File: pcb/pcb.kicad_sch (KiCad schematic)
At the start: 7 parts

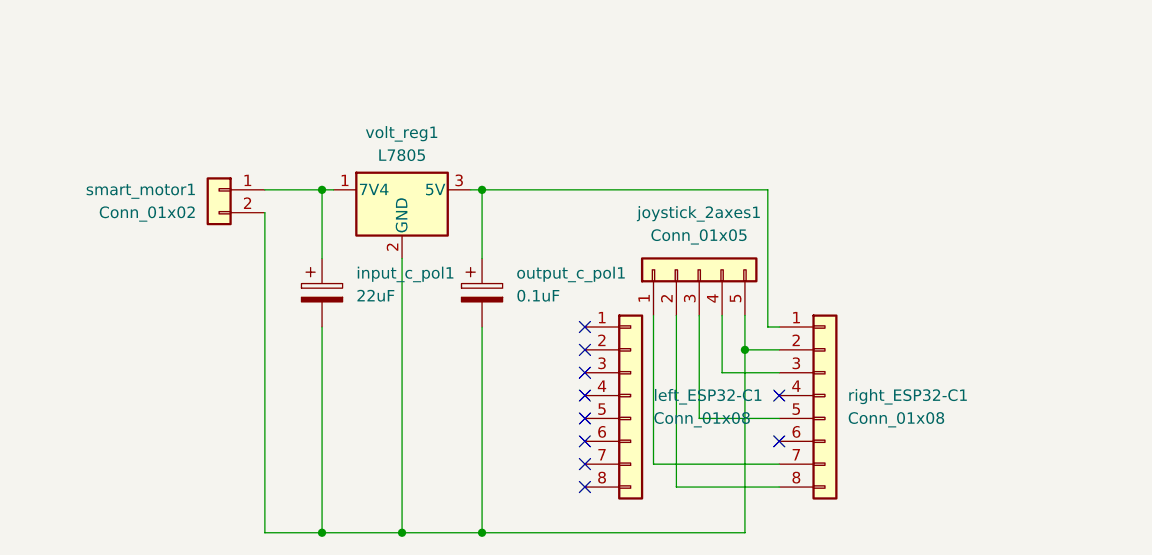
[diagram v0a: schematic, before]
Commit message: added ground plane on front and back of pcb
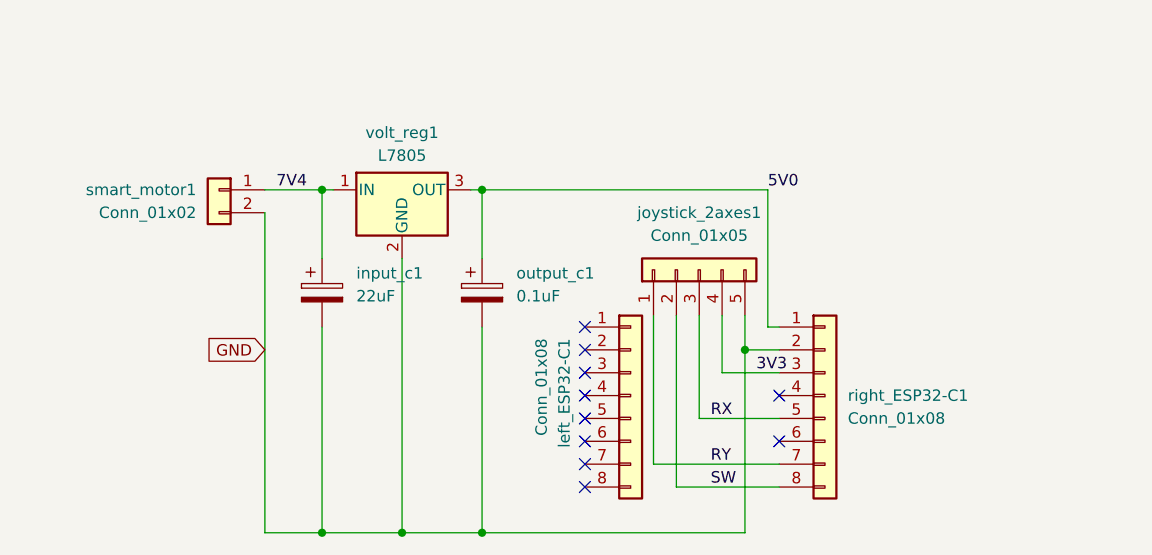
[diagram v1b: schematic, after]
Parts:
- output_c1: renamed from output_c_pol1; footprint Capacitor_THT:CP_Radial_D6.3mm_P2.50mm -> Capacitor_THT:CP_Radial_D4.0mm_P2.00mm
- renumbered input_c_pol1 to input_c1
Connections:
- net 7V4: now reaches input_c1.1, smart_motor1.1 (7V4), volt_reg1.1 (IN)
- net GND: now reaches input_c1.2, joystick_2axes1.5 (GND), output_c1.2, right_ESP32-C1.2 (GND), smart_motor1.2 (GND), volt_reg1.2 (GND)
- net 5V0: now reaches output_c1.1, right_ESP32-C1.1 (5V), volt_reg1.3 (OUT)
- net 3V3: now reaches joystick_2axes1.4 (5V), right_ESP32-C1.3 (3V3)
- net RX: now reaches joystick_2axes1.3 (Rx), right_ESP32-C1.5 (3)
- net RY: now reaches joystick_2axes1.1 (SW), right_ESP32-C1.7 (1)
- net SW: now reaches joystick_2axes1.2 (Ry), right_ESP32-C1.8 (0)
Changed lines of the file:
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@@
+	(wire
+		(pts
+			(xy 134.62 97.79) (xy 148.59 97.79)
+		)
+		(stroke
+			(width 0)
+			(type default)
+		)
+	)
 	(wire
 		(pts
@@
 	(wire
 		(pts
-			(xy 148.59 97.79) (xy 134.62 97.79)
-		)
-		(stroke
-			(width 0)
-			(type default)
-		)
-	)
-	(wire
-		(pts
 			(xy 144.78 81.28) (xy 144.78 85.09)
 		)
@@
 			(width 0)
 			(type default)
+		)
+	)
+	(label "7V4"
+		(at 92.71 67.31 0)
+		(effects
+			(font
+				(size 1.27 1.27)
+			)
+			(justify left bottom)
+		)
+	)
+	(label "RX"
+		(at 140.97 92.71 0)
+		(effects
+			(font
+				(size 1.27 1.27)
+			)
+			(justify left bottom)
+		)
+	)
+	(label "SW"
+		(at 140.97 100.33 0)
+		(effects
+			(font
+				(size 1.27 1.27)
+			)
+			(justify left bottom)
+		)
+	)
+	(label "3V3"
+		(at 146.05 87.63 0)
+		(effects
+			(font
+				(size 1.27 1.27)
+			)
+			(justify left bottom)
+		)
+	)
+	(label "RY"
+		(at 140.97 97.79 0)
+		(effects
+			(font
+				(size 1.27 1.27)
+			)
+			(justify left bottom)
+		)
+	)
+	(label "5V0"
+		(at 147.32 67.31 0)
+		(effects
+			(font
+				(size 1.27 1.27)
+			)
+			(justify left bottom)
+		)
+	)
+	(global_label "GND"
+		(shape input)
+		(at 91.44 85.09 180)
+		(fields_autoplaced yes)
+		(effects
+			(font
+				(size 1.27 1.27)
+			)
+			(justify right)
+		)
+		(property "Intersheetrefs" "${INTERSHEET_REFS}"
+			(at 84.5843 85.09 0)
+			(effects
+				(font
+					(size 1.27 1.27)
+				)
+				(justify right)
+				(hide yes)
+			)
 		)
 	)
@@
 		(dnp no)
 		(fields_autoplaced yes)
-		(property "Reference" "input_c_pol1"
+		(property "Reference" "input_c1"
 			(at 101.6 76.5809 0)
 			(effects
@@
 			(project ""
 				(path "/cf52163e-048c-48d9-89ec-e5d76936dc02"
-					(reference "input_c_pol1")
+					(reference "input_c1")
 					(unit 1)
 				)
@@
 		(dnp no)
 		(property "Reference" "left_ESP32-C1"
-			(at 134.62 90.1699 0)
-			(effects
-				(font
-					(size 1.27 1.27)
-				)
-				(justify left)
+			(at 124.714 83.82 90)
+			(effects
+				(font
+					(size 1.27 1.27)
+				)
+				(justify right)
 			)
 		)
 		(property "Value" "Conn_01x08"
-			(at 134.62 92.7099 0)
-			(effects
-				(font
-					(size 1.27 1.27)
-				)
-				(justify left)
+			(at 122.174 83.82 90)
+			(effects
+				(font
+					(size 1.27 1.27)
+				)
+				(justify right)
 			)
 		)
@@
 		(dnp no)
 		(fields_autoplaced yes)
-		(property "Reference" "output_c_pol1"
+		(property "Reference" "output_c1"
 			(at 119.38 76.5809 0)
 			(effects
@@
 			)
 		)
-		(property "Footprint" "Capacitor_THT:CP_Radial_D6.3mm_P2.50mm"
+		(property "Footprint" "Capacitor_THT:CP_Radial_D4.0mm_P2.00mm"
 			(at 116.5352 82.55 0)
 			(effects
@@
 			(project "pcb"
 				(path "/cf52163e-048c-48d9-89ec-e5d76936dc02"
-					(reference "output_c_pol1")
+					(reference "output_c1")
 					(unit 1)
 				)

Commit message: new pcb with custom footprint
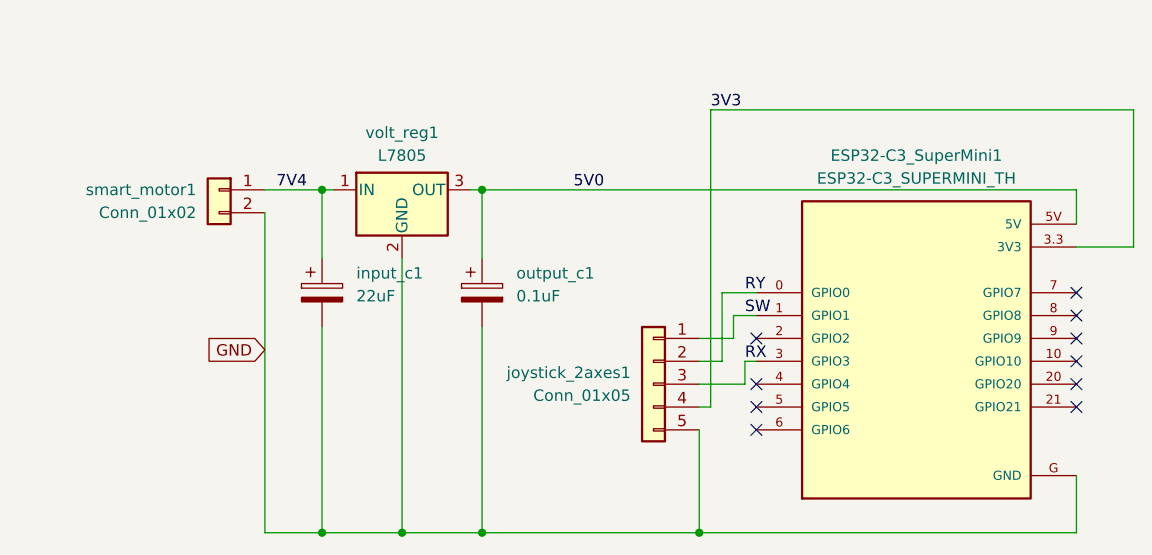
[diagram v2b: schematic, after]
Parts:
- removed left_ESP32-C1, right_ESP32-C1: Conn_01x08, Connector_PinSocket_2.54mm:PinSocket_1x08_P2.54mm_Vertical, symbol Connector_Generic:Conn_01x08
- added ESP32-C3_SuperMini1: ESP32-C3_SUPERMINI_TH, ESP32-C3_SUPERMINI_TH:MODULE_ESP32-C3_SUPERMINI_TH, symbol ESP32-C3_SUPERMINI_TH:ESP32-C3_SUPERMINI_TH
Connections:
- net 3V3: now also ESP32-C3_SuperMini1.3.3 (3V3)
- net 5V0: now also ESP32-C3_SuperMini1.5V
- net GND: now also ESP32-C3_SuperMini1.G (GND)
- net RX: now also ESP32-C3_SuperMini1.3 (GPIO3)
- net RY: now also joystick_2axes1.2 (Ry), ESP32-C3_SuperMini1.0 (GPIO0); no longer joystick_2axes1.1 (SW)
- net SW: now also joystick_2axes1.1 (SW), ESP32-C3_SuperMini1.1 (GPIO1); no longer joystick_2axes1.2 (Ry)
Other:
- moved on the sheet: joystick_2axes1

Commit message: added rounded edges, mounting holes and legend on pcb
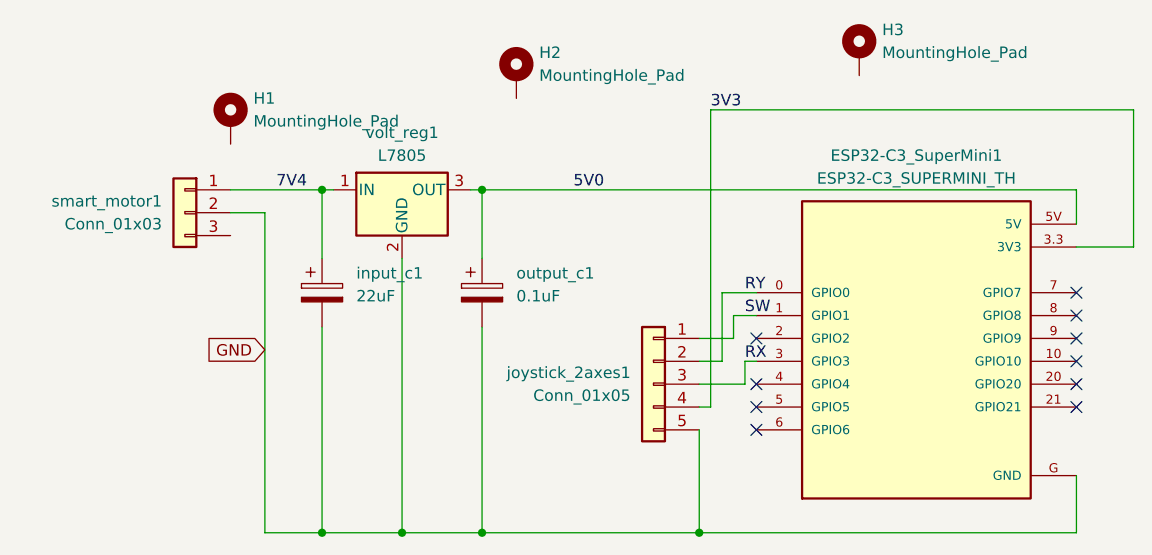
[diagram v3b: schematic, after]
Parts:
- removed smart_motor1: Conn_01x02, Connector_PinHeader_2.54mm:PinHeader_1x02_P2.54mm_Vertical, symbol Connector_Generic:Conn_01x02
- added H1, H2, H3: MountingHole_Pad, MountingHole:MountingHole_2.5mm_Pad, symbol Mechanical:MountingHole_Pad
- added smart_motor1: Conn_01x03, Connector_PinHeader_2.54mm:PinHeader_1x03_P2.54mm_Vertical, symbol Connector_Generic:Conn_01x03
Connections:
- net 7V4: now also smart_motor1.1 (7V4)
- net GND: now also smart_motor1.2 (GND)
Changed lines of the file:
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@@
-	(wire
-		(pts
-			(xy 91.44 67.31) (xy 97.79 67.31)
-		)
-		(stroke
-			(width 0)
-			(type default)
-		)
-	)
 	(wire
 		(pts
@@
 	(wire
 		(pts
+			(xy 87.63 69.85) (xy 91.44 69.85)
+		)
+		(stroke
+			(width 0)
+			(type default)
+		)
+	)
+	(wire
+		(pts
 			(xy 97.79 67.31) (xy 97.79 74.93)
 		)
@@
 		(pts
 			(xy 97.79 82.55) (xy 97.79 105.41)
+		)
+		(stroke
+			(width 0)
+			(type default)
+		)
+	)
+	(wire
+		(pts
+			(xy 87.63 67.31) (xy 97.79 67.31)
 		)
 		(stroke
@@
 	)
 	(symbol
-		(lib_id "Connector_Generic:Conn_01x02")
-		(at 86.36 67.31 0)
-		(mirror y)
+		(lib_id "Mechanical:MountingHole_Pad")
+		(at 157.48 52.07 0)
 		(unit 1)
 		(exclude_from_sim no)
-		(in_bom yes)
+		(in_bom no)
 		(on_board yes)
 		(dnp no)
-		(property "Reference" "smart_motor1"
-			(at 83.82 67.3099 0)
-			(effects
-				(font
-					(size 1.27 1.27)
-				)
-				(justify left)
-			)
-		)
-		(property "Value" "Conn_01x02"
-			(at 83.82 69.8499 0)
-			(effects
-				(font
-					(size 1.27 1.27)
-				)
-				(justify left)
-			)
-		)
-		(property "Footprint" "Connector_PinHeader_2.54mm:PinHeader_1x02_P2.54mm_Vertical"
-			(at 86.36 67.31 0)
+		(fields_autoplaced yes)
+		(property "Reference" "H3"
+			(at 160.02 49.5299 0)
+			(effects
+				(font
+					(size 1.27 1.27)
+				)
+				(justify left)
+			)
+		)
+		(property "Value" "MountingHole_Pad"
+			(at 160.02 52.0699 0)
+			(effects
+				(font
+					(size 1.27 1.27)
+				)
+				(justify left)
+			)
+		)
+		(property "Footprint" "MountingHole:MountingHole_2.5mm_Pad"
+			(at 157.48 52.07 0)
 			(effects
 				(font
@@
 		)
 		(property "Datasheet" "~"
-			(at 86.36 67.31 0)
-			(effects
-				(font
-					(size 1.27 1.27)
-				)
-				(hide yes)
-			)
-		)
-		(property "Description" "Generic connector, single row, 01x02, script generated (kicad-library-utils/schlib/autogen/connector/)"
-			(at 86.36 67.31 0)
-			(effects
-				(font
-					(size 1.27 1.27)
-				)
-				(hide yes)
-			)
-		)
-		(pin "2"
+			(at 157.48 52.07 0)
+			(effects
+				(font
+					(size 1.27 1.27)
+				)
+				(hide yes)
+			)
+		)
+		(property "Description" "Mounting Hole with connection"
+			(at 157.48 52.07 0)
+			(effects
+				(font
+					(size 1.27 1.27)
+				)
+				(hide yes)
+			)
 		)
 		(pin "1"
 		)
 		(instances
-			(project ""
+			(project "pcb"
 				(path "/cf52163e-048c-48d9-89ec-e5d76936dc02"
-					(reference "smart_motor1")
+					(reference "H3")
 					(unit 1)
 				)
@@
 					(unit 1)
 				)
+			)
+		)
+	)
+	(symbol
+		(lib_id "Mechanical:MountingHole_Pad")
+		(at 87.63 59.69 0)
+		(unit 1)
+		(exclude_from_sim no)
+		(in_bom no)
+		(on_board yes)
+		(dnp no)
+		(fields_autoplaced yes)
+		(property "Reference" "H1"
+			(at 90.17 57.1499 0)
+			(effects
+				(font
+					(size 1.27 1.27)
+				)
+				(justify left)
+			)
+		)
+		(property "Value" "MountingHole_Pad"
+			(at 90.17 59.6899 0)
+			(effects
+				(font
+					(size 1.27 1.27)
+				)
+				(justify left)
+			)
+		)
+		(property "Footprint" "MountingHole:MountingHole_2.5mm_Pad"
+			(at 87.63 59.69 0)
+			(effects
+				(font
+					(size 1.27 1.27)
+				)
+				(hide yes)
+			)
+		)
+		(property "Datasheet" "~"
+			(at 87.63 59.69 0)
+			(effects
+				(font
+					(size 1.27 1.27)
+				)
+				(hide yes)
+			)
+		)
+		(property "Description" "Mounting Hole with connection"
+			(at 87.63 59.69 0)
+			(effects
+				(font
+					(size 1.27 1.27)
+				)
+				(hide yes)
+			)
+		)
+		(pin "1"
+		)
+		(instances
+			(project ""
+				(path "/cf52163e-048c-48d9-89ec-e5d76936dc02"
+					(reference "H1")
+					(unit 1)
+				)
+			)
+		)
+	)
+	(symbol
+		(lib_id "Connector_Generic:Conn_01x03")
+		(at 82.55 69.85 0)
+		(mirror y)
+		(unit 1)
+		(exclude_from_sim no)
+		(in_bom yes)
+		(on_board yes)
+		(dnp no)
+		(property "Reference" "smart_motor1"
+			(at 80.01 68.5799 0)
+			(effects
+				(font
+					(size 1.27 1.27)
+				)
+				(justify left)
+			)
+		)
+		(property "Value" "Conn_01x03"
+			(at 80.01 71.1199 0)
+			(effects
+				(font
+					(size 1.27 1.27)
+				)
+				(justify left)
+			)
+		)
+		(property "Footprint" "Connector_PinHeader_2.54mm:PinHeader_1x03_P2.54mm_Vertical"
+			(at 82.55 69.85 0)
+			(effects
+				(font
+					(size 1.27 1.27)
+				)
+				(hide yes)
+			)
+		)
+		(property "Datasheet" "~"
+			(at 82.55 69.85 0)
+			(effects
+				(font
+					(size 1.27 1.27)
+				)
+				(hide yes)
+			)
+		)
+		(property "Description" "Generic connector, single row, 01x03, script generated (kicad-library-utils/schlib/autogen/connector/)"
+			(at 82.55 69.85 0)
+			(effects
+				(font
+					(size 1.27 1.27)
+				)
+				(hide yes)
+			)
+		)
+		(pin "2"
+		)
+		(pin "1"
+		)
+		(pin "3"
+		)
+		(instances
+			(project ""
+				(path "/cf52163e-048c-48d9-89ec-e5d76936dc02"
+					(reference "smart_motor1")
+					(unit 1)
+				)
+			)
+		)
+	)
+	(symbol
+		(lib_id "Mechanical:MountingHole_Pad")
+		(at 119.38 54.61 0)
+		(unit 1)
+		(exclude_from_sim no)
+		(in_bom no)
+		(on_board yes)
+		(dnp no)
+		(fields_autoplaced yes)
+		(property "Reference" "H2"
+			(at 121.92 52.0699 0)
+			(effects
+				(font
+					(size 1.27 1.27)
+				)
+				(justify left)
+			)
+		)
+		(property "Value" "MountingHole_Pad"
+			(at 121.92 54.6099 0)
+			(effects
+				(font
+					(size 1.27 1.27)
+				)
+				(justify left)
+			)
+		)
+		(property "Footprint" "MountingHole:MountingHole_2.5mm_Pad"
+			(at 119.38 54.61 0)
+			(effects
+				(font
+					(size 1.27 1.27)
+				)
+				(hide yes)
+			)
+		)
+		(property "Datasheet" "~"
+			(at 119.38 54.61 0)
+			(effects
+				(font
+					(size 1.27 1.27)
+				)
+				(hide yes)
+			)
+		)
+		(property "Description" "Mounting Hole with connection"
+			(at 119.38 54.61 0)
+			(effects
+				(font
+					(size 1.27 1.27)
+				)
+				(hide yes)
+			)
+		)
+		(pin "1"
+		)
+		(instances
+			(project "pcb"
+				(path "/cf52163e-048c-48d9-89ec-e5d76936dc02"
+					(reference "H2")
+					(unit 1)
+				)
